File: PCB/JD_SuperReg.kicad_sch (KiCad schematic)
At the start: 64 parts, among them Q101 D44H11, Q102 BC556, Q103 D45H11, Q104 BC546, T1 18V + 18V, T2 Transformer_SP_1S, U101 AD825ARZ, U102 AD825ARZ

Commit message: Finalized layout
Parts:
- removed C111, C112: 100pF, Capacitor_THT:C_Disc_D4.7mm_W2.5mm_P5.00mm, symbol Device:C_Small
- removed C15, C16, C17, C18: 120uF, Capacitor_THT:CP_Radial_D10.0mm_P5.00mm, symbol Device:C_Polarized_Small
- removed C3: 0.01uF, Capacitor_THT:C_Rect_L7.2mm_W2.5mm_P5.00mm_FKS2_FKP2_MKS2_MKP2, symbol Device:C_Small
- removed C4, C5, C7, C8: 2200uF, Capacitor_THT:CP_Radial_D18.0mm_P7.50mm, symbol Device:C_Small
- removed C6: 0.15uF, Capacitor_THT:C_Rect_L7.2mm_W3.5mm_P5.00mm_FKS2_FKP2_MKS2_MKP2, symbol Device:C_Small
- removed D101, D106: LED_Small, LED_THT:LED_D3.0mm, symbol Device:LED_Small
- removed D102, D107: D_Zener_Small, Diode_THT:D_DO-35_SOD27_P10.16mm_Horizontal, symbol Device:D_Zener_Small
- removed D103, D104, D108, D109: D_Small, Diode_THT:D_DO-35_SOD27_P10.16mm_Horizontal, symbol Device:D_Small
- removed D105, D110: LM329, Package_TO_SOT_THT:TO-92_Inline, symbol Super-Regulator-Combined-rescue:LM329Z
- removed HS101, HS102: Heatsink, Heatsink:Heatsink_Fischer_SK104-STCB_35x13mm__2xDrill3.5mm_ScrewM3, symbol Mechanical:Heatsink
- removed Q101: D44H11, Package_TO_SOT_THT:TO-220-3_Vertical, symbol Device:Q_PNP_BCE
- removed Q102: BC556, Package_TO_SOT_THT:TO-92_Inline, symbol Transistor_BJT:BC556
- removed Q103: D45H11, Package_TO_SOT_THT:TO-220-3_Vertical, symbol Device:Q_NPN_BCE
- removed Q104: BC546, Package_TO_SOT_THT:TO-92_Inline, symbol Transistor_BJT:BC546
- removed R101, R108: 249R, Resistor_THT:R_Axial_DIN0207_L6.3mm_D2.5mm_P10.16mm_Horizontal, symbol Device:R_Small
- removed R102, R109: 10K, Resistor_THT:R_Axial_DIN0207_L6.3mm_D2.5mm_P10.16mm_Horizontal, symbol Device:R_Small
- removed R103, R110: 10R, Resistor_THT:R_Axial_DIN0207_L6.3mm_D2.5mm_P10.16mm_Horizontal, symbol Device:R_Small
- removed R104, R111: 499R, Resistor_THT:R_Axial_DIN0207_L6.3mm_D2.5mm_P10.16mm_Horizontal, symbol Device:R_Small
- removed R105, R112: 4.99K, Resistor_THT:R_Axial_DIN0207_L6.3mm_D2.5mm_P10.16mm_Horizontal, symbol Device:R_Small
- removed R106, R107, R113, R114: 1K, Resistor_THT:R_Axial_DIN0207_L6.3mm_D2.5mm_P10.16mm_Horizontal, symbol Device:R_Small
- removed R115, R116: 100R, Resistor_THT:R_Axial_DIN0207_L6.3mm_D2.5mm_P10.16mm_Horizontal, symbol Device:R_Small
- removed T1: 18V + 18V, Super-Regulator Combined Dual:Talema-25VA-Transformer, symbol Super-Regulator-Combined-rescue:TalemaTransformer
- removed T2: Transformer_SP_1S, symbol Device:Transformer_SP_1S
- removed U101, U102: AD825ARZ, Package_SO:SOIC-8_3.9x4.9mm_P1.27mm, symbol Super-Regulator-Combined-rescue:AD825ARZ
- added C3, C4: 4700u, Capacitor_THT:CP_Radial_D18.0mm_P7.50mm, symbol Device:C_Polarized_Small
- added C5, C6, C7, C8: 150u, Capacitor_THT:CP_Radial_D8.0mm_P3.50mm, symbol Device:C_Polarized_Small
- added D10, D15, D16, D17, D18, D9: 9V1, Diode_SMD:D_SOD-123, symbol Device:D_Zener_Small
- added D11, D12, D13, D14: 4148, Diode_SMD:D_SOD-123, symbol Device:D_Small
- added D5, D6, D7, D8: SBYV27, Diode_THT:D_DO-15_P10.16mm_Horizontal, symbol Device:D_Small
- added H1, H2, H3, H4: M3, Ariamelon-HolePad:MountingHole_3.2mm_M3_Pad, symbol Mechanical:MountingHole
- added HS1, HS2: Heatsink, Ariamelon-Misc:Heatsink, symbol Mechanical:Heatsink
- added J1: V+_In, TerminalBlock_Phoenix:TerminalBlock_Phoenix_MKDS-1,5-2-5.08_1x02_P5.08mm_Horizontal, symbol Connector:Screw_Terminal_01x02
- added J2: V-_In, TerminalBlock_Phoenix:TerminalBlock_Phoenix_MKDS-1,5-2-5.08_1x02_P5.08mm_Horizontal, symbol Connector:Screw_Terminal_01x02
- added J3: Out, Ariamelon-Connector:TerminalBlock_Phoenix_MKDS-1,5-8-5.08_1x08_P5.08mm_Horizontal, symbol Ariamelon-Connector:Screw_Terminal_01x04_2x
- added J4: V+_Jumper, Ariamelon-Header:PinHeader_1x04_P2.54mm_Vertical_Jumper, symbol Connector_Generic:Conn_01x04
- added J5: V-_Jumper, Ariamelon-Header:PinHeader_1x04_P2.54mm_Vertical_Jumper, symbol Connector_Generic:Conn_01x04
- added Q1, Q9: BCM857DS, Ariamelon-Package:SOT-23-6, symbol Device:Q_Dual_PNP_PNP_E1B1C2E2B2C1
- added Q10, Q2: BCM847DS, Ariamelon-Package:SOT-23-6, symbol Device:Q_Dual_NPN_NPN_E1B1C2E2B2C1
- added Q3: D44H11, Ariamelon-Package:TO-220-3_TO-247_Combined_Vertical, symbol Device:Q_NPN_BCE
- added Q4: D45H11, Ariamelon-Package:TO-220-3_TO-247_Combined_Vertical, symbol Device:Q_PNP_BCE
- added Q5: ZXTP2041F, Ariamelon-Package:SOT-23-3, symbol Transistor_BJT:BC857
- added Q6: ZXTN2040F, Ariamelon-Package:SOT-23-3, symbol Transistor_BJT:BC847
- added R11, R6: 100, Resistor_SMD:R_MiniMELF_MMA-0204, symbol Device:R_Small
- added R12, R5: 120, Resistor_SMD:R_MiniMELF_MMA-0204, symbol Device:R_Small
- added R13, R14, R3, R4: 10K, Resistor_SMD:R_MiniMELF_MMA-0204, symbol Device:R_Small
- added R15, R18: 1k2, Resistor_SMD:R_MiniMELF_MMA-0204, symbol Device:R_Small
- added R16, R17: 1k5, Resistor_SMD:R_MiniMELF_MMA-0204, symbol Device:R_Small
- added R7, R8: 4k7, Resistor_SMD:R_MiniMELF_MMA-0204, symbol Device:R_Small
- added U1, U2: ADA4522, Ariamelon-Package:SOIC-8_3.9x4.9mm_P1.27mm, symbol Ariamelon-IC:Opamp_Single
- C1: value 0.15uF -> 100n; footprint Capacitor_THT:C_Rect_L7.2mm_W3.5mm_P5.00mm_FKS2_FKP2_MKS2_MKP2 -> Ariamelon-Device:C_1206_3216Metric
- C10, C11, C12, C13, C14, C9: value 120uF -> 150u; footprint Capacitor_THT:CP_Radial_D10.0mm_P5.00mm -> Capacitor_THT:CP_Radial_D8.0mm_P3.50mm; Manufacturer No. (none) -> EEU-FC1V151
- C2: value 0.01uF -> 100n; footprint Capacitor_THT:C_Rect_L7.2mm_W2.5mm_P5.00mm_FKS2_FKP2_MKS2_MKP2 -> Ariamelon-Device:C_1206_3216Metric
- D1: value SB180 -> SBYV27; footprint Diode_THT:D_DO-41_SOD81_P10.16mm_Horizontal -> Diode_THT:D_DO-15_P10.16mm_Horizontal
- D2, D3, D4: value D_Small -> SBYV27; footprint Diode_THT:D_DO-41_SOD81_P10.16mm_Horizontal -> Diode_THT:D_DO-15_P10.16mm_Horizontal
- F1, F2: footprint HP_Footprints:5x20mm-BK-1A3399-01-fuseholder -> Fuse:Fuseholder_Cylinder-5x20mm_Schurter_0031_8201_Horizontal_Open
- R1, R2: value 32R -> 10; footprint Resistor_THT:R_Axial_DIN0207_L6.3mm_D2.5mm_P10.16mm_Horizontal -> Resistor_SMD:R_MiniMELF_MMA-0204
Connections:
- net VCC: now reaches C9.1
- net VCC: now also J3.8 (Pin_8), J4.1 (Pin_1), Q3.3 (E), U1.7 (V+)
- net GND: now reaches C9.2
- net GND: now also C10.1, C3.2, C4.1, C5.2, C6.1, D5.2 (A), D6.2 (A), D7.1 (K), D8.1 (K), J3.4 (Pin_4), J3.5 (Pin_5), J4.4 (Pin_4), J5.1 (Pin_1), Q5.3 (C), Q6.3 (C), R3.2, R4.2, U1.4 (V-), U2.7 (V+)
- net at C11.1: now also D11.2 (A), D13.1 (K), R7.1, U1.3 (+)
- net at C11.2: now also D16.2 (A), J3.6 (Pin_6), J4.3 (Pin_3), R13.2, R16.2
- net at D2.1 (K): now also D1.1 (K), F1.1
- net at D2.2 (A): now also R1.2, D6.1 (K), J1.2 (Pin_2)
- net at C12.1: now also D17.2 (A), J3.3 (Pin_3), J5.2 (Pin_2), R14.1, R17.1
- net at C12.2: now also D12.2 (A), D14.1 (K), R8.1, U2.3 (+)
- net at F2.1: now also D3.2 (A), D4.2 (A)
- net at F2.2: now also C4.2, C6.2, Q2.4 (E2), Q4.2 (C), R6.2
- net at R2.2: now also D3.1 (K), D7.2 (A), J2.1 (Pin_1)
- net VEE: now reaches C10.2
- net VEE: now also J3.1 (Pin_1), J5.4 (Pin_4), Q4.3 (E), U2.4 (V-)
- net at D1.2 (A): now also C1.1, D5.1 (K), J1.1 (Pin_1)
- net at D4.1 (K): now also C2.1, D8.2 (A), J2.2 (Pin_2)
- net at C13.1: now also J3.7 (Pin_7), J4.2 (Pin_2), Q9.4 (E2), R11.1, R15.1
- net at C13.2: now also D11.1 (K), D13.2 (A), R15.2, R16.1, U1.2 (-)
- net at C14.1: now also D12.1 (K), D14.2 (A), R17.2, R18.1, U2.2 (-)
- net at C14.2: now also J3.2 (Pin_2), J5.3 (Pin_3), Q10.4 (E2), R12.2, R18.2
- net at F1.2: now also C3.1, C5.1, Q1.4 (E2), Q3.2 (C), R5.2
- net V1-COM: no longer names the net of C2.2, R2.1
- net V1-COM: no longer R1.2
- new net: Q2.1 (E1), Q2.5 (B2), R6.1
- new net: D15.1 (K), D16.1 (K)
- new net: C7.1, D9.1 (K), Q1.6 (C1), Q3.1 (B)
- new net: Q1.1 (E1), Q1.5 (B2), R5.1
- new net: Q1.2 (B1), Q1.3 (C2), R3.1
- new net: Q2.2 (B1), Q2.3 (C2), R4.1
- new net: D15.2 (A), Q9.6 (C1), R7.2
- new net: D17.1 (K), D18.1 (K)
- new net: D18.2 (A), Q10.6 (C1), R8.2
- new net: Q10.1 (E1), Q10.5 (B2), R12.1
- new net: Q10.2 (B1), Q10.3 (C2), R14.2
- new net: C8.1, D10.1 (K), Q6.2 (E)
- new net: C8.2, D10.2 (A), Q2.6 (C1), Q4.1 (B)
- new net: Q5.1 (B), U1.6
- new net: C7.2, D9.2 (A), Q5.2 (E)
- new net: Q9.2 (B1), Q9.3 (C2), R13.1
- new net: Q9.1 (E1), Q9.5 (B2), R11.2
- new net: Q6.1 (B), U2.6

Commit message: Initial public upload
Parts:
- removed J4: V+_Jumper, Ariamelon-Header:PinHeader_1x04_P2.54mm_Vertical_Jumper, symbol Connector_Generic:Conn_01x04
- removed J5: V-_Jumper, Ariamelon-Header:PinHeader_1x04_P2.54mm_Vertical_Jumper, symbol Connector_Generic:Conn_01x04
- added C15, C16: 100p, Ariamelon-Device:C_0805_2012Metric, symbol Device:C_Small
- added J4: V+_Sen+_Jumper, Ariamelon-Header:PinHeader_1x02_P2.54mm_Vertical_Jumper, symbol Connector_Generic:Conn_01x02
- added J5: V+_Sen-_Jumper, Ariamelon-Header:PinHeader_1x02_P2.54mm_Vertical_Jumper, symbol Connector_Generic:Conn_01x02
- added J6: V-_Sen+_Jumper, Ariamelon-Header:PinHeader_1x02_P2.54mm_Vertical_Jumper, symbol Connector_Generic:Conn_01x02
- added J7: V-_Sen-_Jumper, Ariamelon-Header:PinHeader_1x02_P2.54mm_Vertical_Jumper, symbol Connector_Generic:Conn_01x02
- added R10, R9: 120, Resistor_SMD:R_MiniMELF_MMA-0204, symbol Device:R_Small
- added RV1, RV2: 1k, Potentiometer_THT:Potentiometer_Bourns_3266W_Vertical, symbol Device:R_Potentiometer_Small
- C1, C2: Manufacturer No. (none) -> 12061C104KAT2A; Voltage (none) -> 100V
- C10, C11, C12, C13, C14, C3, C4, C5, C6, C7, C8, C9: Voltage (none) -> 35V
- D1, D2, D3, D4, D5, D6, D7, D8: Manufacturer No. (none) -> SBYV27-200-E3/54
- F1, F2: Manufacturer No. (none) -> 0031.8201
- H1, H2, H3, H4: now left out of the parts list
- J3: Manufacturer No. (none) -> 1715721
- Q1, Q9: Manufacturer No. (none) -> BCM857DS
- Q10, Q2: Manufacturer No. (none) -> BCM847DS
- Q3: value D44H11 -> BDW93C; symbol Device:Q_NPN_BCE -> Device:Q_NPN_Darlington_BCE; Manufacturer No. (none) -> BDW93C
- Q4: value D45H11 -> BDW94C; symbol Device:Q_PNP_BCE -> Device:Q_PNP_Darlington_BCE; Manufacturer No. (none) -> BDW94C
- Q5: value ZXTP2041F -> MMBT5087; Manufacturer No. (none) -> MMBT5087LT1G
- Q6: value ZXTN2040F -> MMBT5089; Manufacturer No. (none) -> MMBT5089LT1G
- R1, R2: Manufacturer No. (none) -> MMA02040C1009FB300
- R11, R6: value 100 -> 120; Manufacturer No. (none) -> MMA02040C1200FB300
- R12, R5: Manufacturer No. (none) -> MMA02040C1200FB300
- R13, R14, R3, R4: Manufacturer No. (none) -> MMA02040C1002FB300
- R15, R18: value 1k2 -> 560; Manufacturer No. (none) -> MMA02040C5600FB300
- R16, R17: value 1k5 -> 560; Manufacturer No. (none) -> MMA02040C5600FB300
- R7, R8: value 4k7 -> 10K; Manufacturer No. (none) -> MMA02040C1002FB300
- U1, U2: Manufacturer No. (none) -> ADA4522-1ARZ-R7
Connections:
- net GND: now also J5.2 (Pin_2), J6.1 (Pin_1)
- net VCC: now also J4.1 (Pin_1)
- net VEE: now also J7.2 (Pin_2)
- net at C13.2, D11.1 (K), D13.2 (A)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: now also RV1.2; no longer R15.2, R16.1
- net at C11.1, D11.2 (A), D13.1 (K)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: now also R7.2; no longer R7.1
- net at C11.2, D16.2 (A), J3.6 (Pin_6)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: now also C15.2, J5.1 (Pin_1)
- net at D15.2 (A), Q9.6 (C1): now also R7.1; no longer R7.2
- net at C14.2, Q10.4 (E2), R12.2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: now also C16.1, R10.1; no longer J3.2 (Pin_2)
- net at C12.1, D17.2 (A), J3.3 (Pin_3)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: now also C16.2, J6.2 (Pin_2)
- net at C13.1, Q9.4 (E2), R11.1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: now also C15.1, R9.1; no longer J3.7 (Pin_7)
- net at C14.1, D12.1 (K), D14.2 (A)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: now also RV2.2; no longer R17.2, R18.1
- new net: J3.2 (Pin_2), J7.1 (Pin_1), R10.2
- new net: J3.7 (Pin_7), J4.2 (Pin_2), R9.2
- new net: R18.1, RV2.1
- new net: R16.1, RV1.3
- new net: R15.2, RV1.1
- new net: R17.2, RV2.3
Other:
- company: (none) -> Laid out by Ariamelon (https://github.com/Ariamelon/JD_SuperReg)
- title: (none) -> Jung/Didden Super Regulator
- moved on the sheet: C1, C10, C11, C12, C13, C14, C2, C3, C4, C5, C6, C7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

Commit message: 27/09/2023 update
Changed board to 4 layers. Removed fuses. Added MOV surge protection and resistors for RC input filter.
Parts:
- removed D1, D2, D3, D4, D5, D6, D7, D8: SBYV27, Diode_THT:D_DO-15_P10.16mm_Horizontal, symbol Device:D_Small
- removed F1, F2: Fuse_Small, Fuse:Fuseholder_Cylinder-5x20mm_Schurter_0031_8201_Horizontal_Open, symbol Device:Fuse_Small
- removed J1: V+_In, TerminalBlock_Phoenix:TerminalBlock_Phoenix_MKDS-1,5-2-5.08_1x02_P5.08mm_Horizontal, symbol Connector:Screw_Terminal_01x02
- removed J2: V-_In, TerminalBlock_Phoenix:TerminalBlock_Phoenix_MKDS-1,5-2-5.08_1x02_P5.08mm_Horizontal, symbol Connector:Screw_Terminal_01x02
- removed J3: Out, Ariamelon-Connector:TerminalBlock_Phoenix_MKDS-1,5-8-5.08_1x08_P5.08mm_Horizontal, symbol Ariamelon-Connector:Screw_Terminal_01x04_2x
- added D1, D2: 4A, Diode_THT:Diode_Bridge_Vishay_GBU, symbol Device:D_Bridge_+AA-
- added J1: In, TerminalBlock_Phoenix:TerminalBlock_Phoenix_MKDS-1,5-4-5.08_1x04_P5.08mm_Horizontal, symbol Connector:Screw_Terminal_01x04
- added J2: Out, Ariamelon-Connector:TerminalBlock_Phoenix_MKDS-1,5-8-5.08_1x08_P5.08mm_Horizontal, symbol Connector:Screw_Terminal_01x08
- added R3, R4, R5, R6: 4R7, Resistor_THT:R_Axial_DIN0617_L17.0mm_D6.0mm_P20.32mm_Horizontal, symbol Device:R_Small
- added TH1, TH2: 40VAC, Varistor:RV_Disc_D9mm_W5.2mm_P5mm, symbol Ariamelon-Device:Thermistor_Small
- J3: renamed from J4; value V+_Sen+_Jumper -> V+_Sen+
- J4: renamed from J5; value V+_Sen-_Jumper -> V+_Sen-
- J5: renamed from J6; value V-_Sen+_Jumper -> V-_Sen+
- J6: renamed from J7; value V-_Sen-_Jumper -> V-_Sen-
- renumbered D16 to D10, D17 to D11, D18 to D12, D9 to D3, D10 to D4, D11 to D5, D12 to D6, D13 to D7, D14 to D8, D15 to D9, Q9 to Q7, Q10 to Q8, R6 to R10, R7 to R11, R8 to R12, R11 to R13, R12 to R14, R13 to R15, R14 to R16, R15 to R17, R16 to R18, R17 to R19, R18 to R20, R9 to R21, R10 to R22, R3 to R7, R4 to R8, R5 to R9
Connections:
- net GND: now also D1.4 (-), D2.1 (+), J2.4 (Pin_4), J2.5 (Pin_5)
- net VCC: now also J2.8 (Pin_8)
- net VEE: now also J2.1 (Pin_1)
- net at R1.2: now also D1.3, J1.2 (Pin_2), TH1.2
- net at C4.2, C6.2, Q2.4 (E2)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: now also R4.2, R6.2
- net at C11.2, C15.2, D10.2 (A)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: now also J2.6 (Pin_6)
- net at C2.1: now also D2.3, J1.4 (Pin_4), TH2.1
- net at R2.2: now also D2.2, J1.3 (Pin_3), TH2.2
- net at C1.1: now also D1.2, J1.1 (Pin_1), TH1.1
- net at C3.1, C5.1, Q1.4 (E2)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: now also R3.2, R5.2
- net at J6.1 (Pin_1), R22.2: now also J2.2 (Pin_2)
- net at C12.1, C16.2, D11.2 (A)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: now also J2.3 (Pin_3)
- net at J3.2 (Pin_2), R21.2: now also J2.7 (Pin_7)
- new net: D2.4 (-), R4.1, R6.1
- new net: D1.1 (+), R3.1, R5.1
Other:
- moved on the sheet: C1, C10, C11, C12, C13, C14, C15, C16, C2, C3, C4, C5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

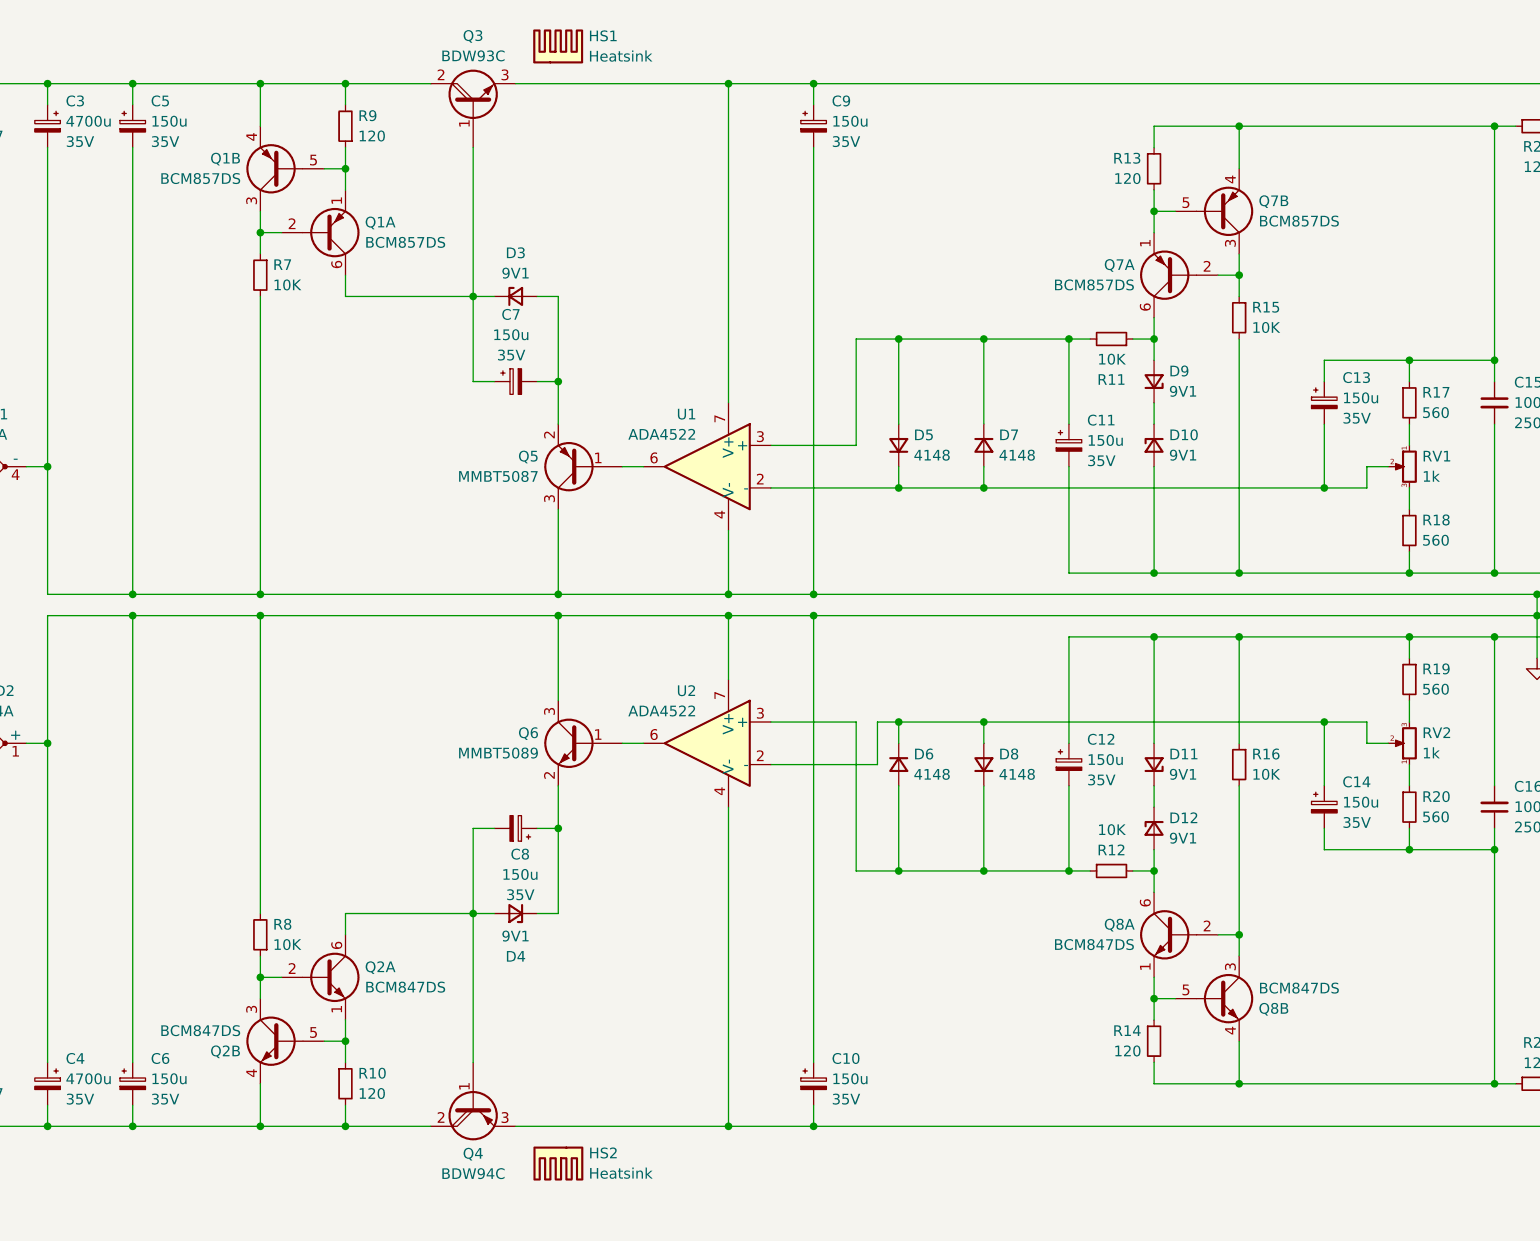
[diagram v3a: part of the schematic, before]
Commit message: 05/10/2023 update
Changed output voltage to 15V.
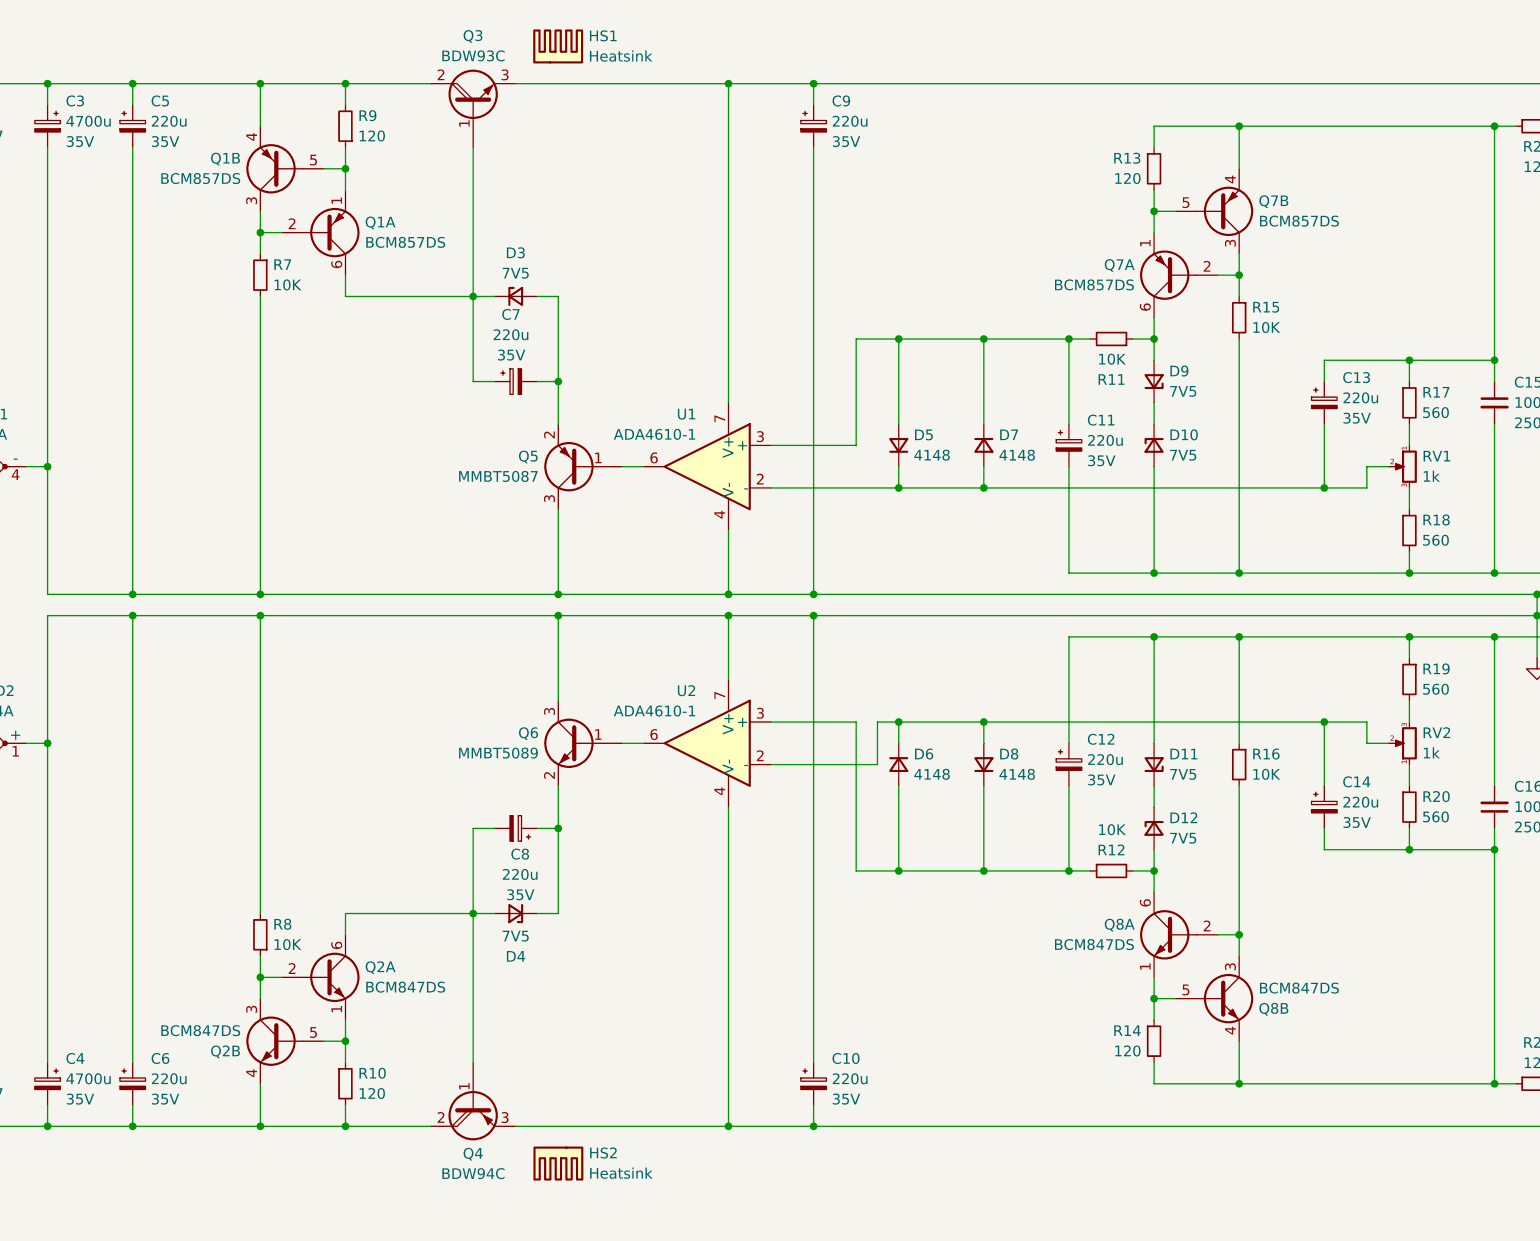
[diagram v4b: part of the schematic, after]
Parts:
- C1, C2: Manufacturer No. 12061C104KAT2A -> GCM21BR72A104KA37L
- C10, C11, C12, C13, C14, C5, C6, C7, C8, C9: value 150u -> 220u; Manufacturer No. EEU-FC1V151 -> EEUFR1V221
- C3, C4: Manufacturer No. B41888C7478M000 -> EKYB350ELL472MMN3S
- D10, D11, D12, D3, D4, D9: value 9V1 -> 7V5; Manufacturer No. MMSZ5239BT1G -> MMSZ5236BT1G
- R1, R2: Manufacturer No. MMA02040C1009FB300 -> RC1206JR-0710RL
- U1, U2: value ADA4522 -> ADA4610-1; Manufacturer No. ADA4522-1ARZ-R7 -> ADA4610-1ARZ-R7
